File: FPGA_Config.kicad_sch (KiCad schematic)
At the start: 1 part

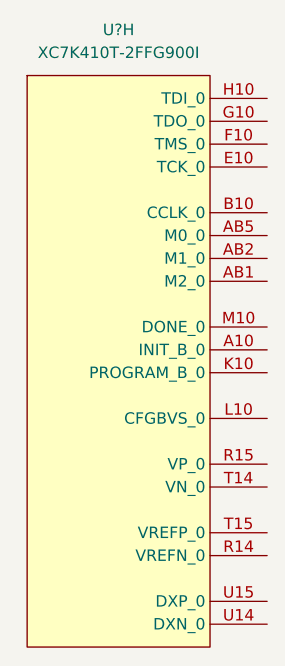
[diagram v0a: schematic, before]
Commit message: Add MT41K512M8DA DDR3L
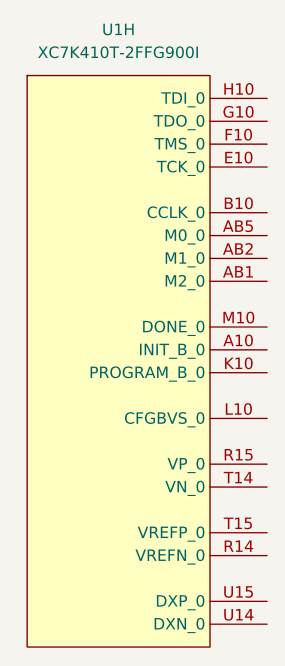
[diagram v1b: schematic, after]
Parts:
- gave numbers to parts that had none: 1
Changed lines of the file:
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@@
   (symbol (lib_id "antmicroMicrocontrollers:XC7K410T-2FFG900I") (at 215.9 146.05 0) (unit 8)
     (in_bom yes) (on_board yes) (fields_autoplaced)
-    (property "Reference" "U?" (id 0) (at 215.9 107.95 0))
+    (property "Reference" "U1" (id 0) (at 215.9 107.95 0))
     (property "Value" "XC7K410T-2FFG900I" (id 1) (at 215.9 110.49 0))
     (property "Footprint" "antmicro-footprints:xc7k410t-2ffg900I" (id 2) (at 215.9 220.98 0)

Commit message: Unify title block
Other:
- title: (none) -> K410T devboard
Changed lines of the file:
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@@
   (paper "A3")
   (title_block
-    (comment 1 "www.antmicro.com")
-    (comment 2 "Antmicro Ltd")
+    (title "K410T devboard")
+    (date "2022-12-20")
+    (rev "0.0.99")
   )
   (symbol (lib_id "antmicroMicrocontrollers:XC7K410T-2FFG900I") (at 215.9 146.05 0) (unit 8)
